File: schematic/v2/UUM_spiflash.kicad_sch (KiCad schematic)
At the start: 17 parts, among them U21 74HC4050D, U22 AP2112K-3.3, U23 W25Q128JVS, U24 74HC4050D, U25 AP2112K-3.3, U26 W25Q128JVS, U28 74LVC1G3157

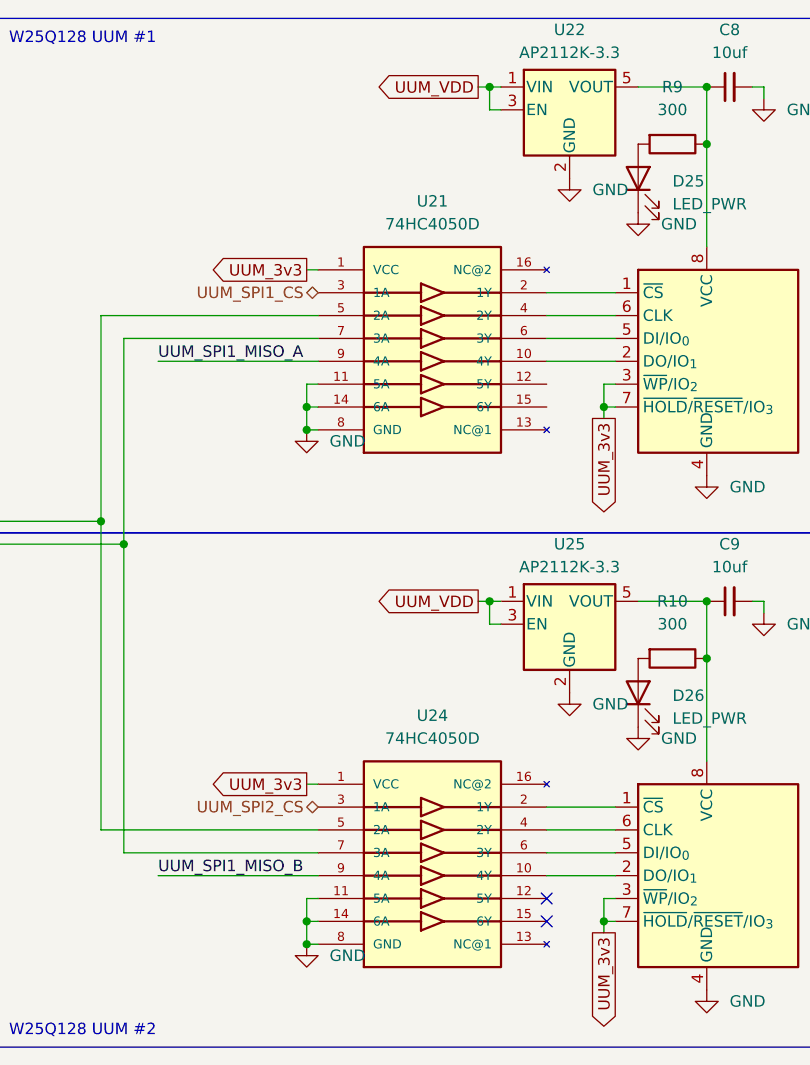
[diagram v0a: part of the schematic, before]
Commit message: need to update PCB and new traces
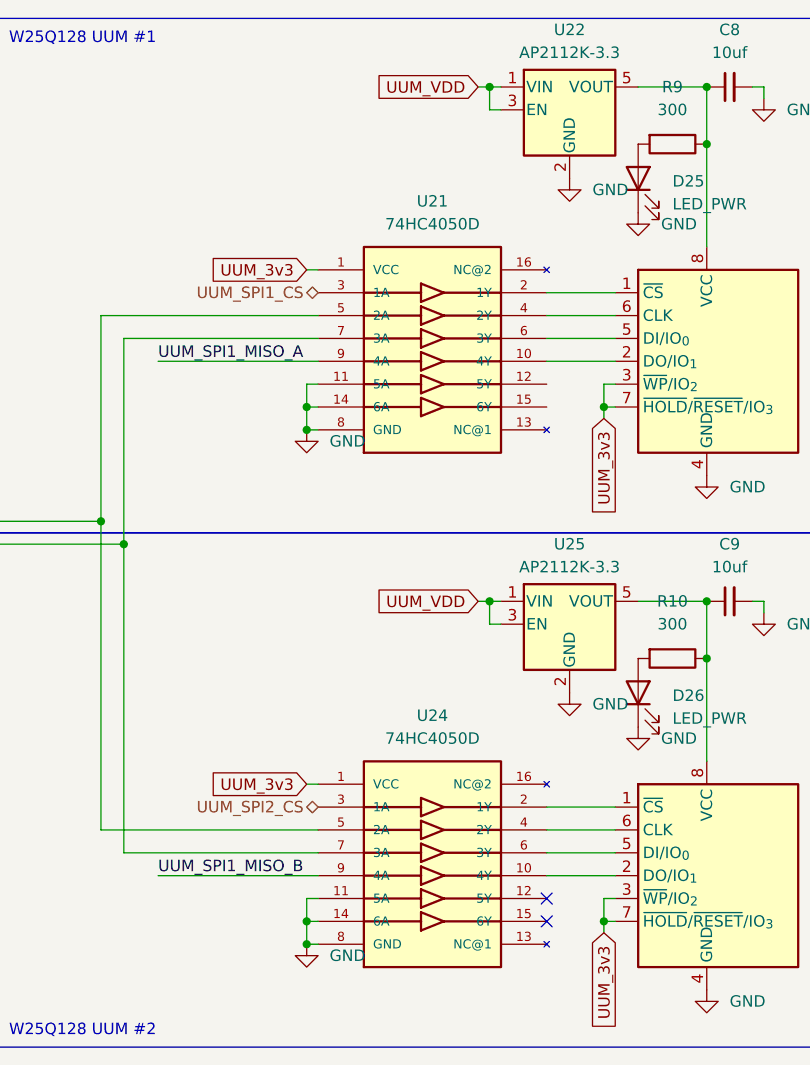
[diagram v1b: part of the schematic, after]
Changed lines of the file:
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@@
 	)
 	(global_label "UUM_3v3"
-		(shape output)
+		(shape input)
 		(at 90.17 123.19 180)
 		(fields_autoplaced yes)
@@
 	)
 	(global_label "UUM_3v3"
-		(shape output)
+		(shape input)
 		(at 123.19 82.55 270)
 		(fields_autoplaced yes)
@@
 	)
 	(global_label "UUM_VDD"
-		(shape output)
+		(shape input)
 		(at 109.22 45.72 180)
 		(fields_autoplaced yes)
@@
 	)
 	(global_label "UUM_VDD"
-		(shape output)
+		(shape input)
 		(at 109.22 102.87 180)
 		(fields_autoplaced yes)
@@
 	)
 	(global_label "UUM_3v3"
-		(shape output)
+		(shape input)
 		(at 123.19 139.7 270)
 		(fields_autoplaced yes)
@@
 	)
 	(global_label "UUM_3v3"
-		(shape output)
+		(shape input)
 		(at 90.17 66.04 180)
 		(fields_autoplaced yes)

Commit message: time to start routing?
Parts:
- D27: value LED_PWR -> SPI_SEL
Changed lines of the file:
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@@
 			)
 		)
-		(property "Value" "LED_PWR"
+		(property "Value" "SPI_SEL"
 			(at 189.23 80.9624 90)
 			(effects
